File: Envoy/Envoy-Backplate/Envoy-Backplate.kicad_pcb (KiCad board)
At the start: 2 copper layers, 95.4 x 95.4 mm, 13 parts

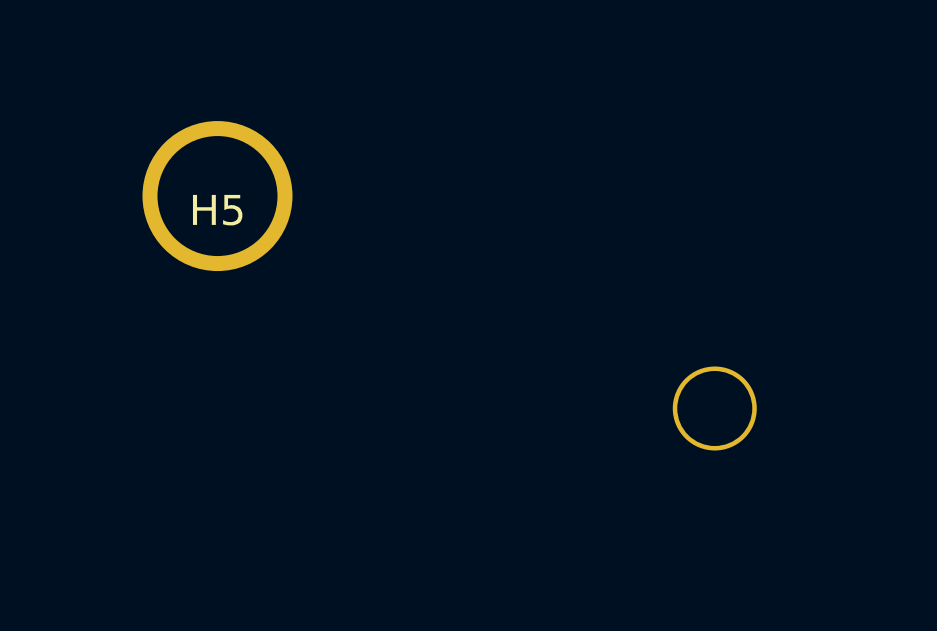
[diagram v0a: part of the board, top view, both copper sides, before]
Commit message: Move standoff and bumper positioning to make the backplate work easier
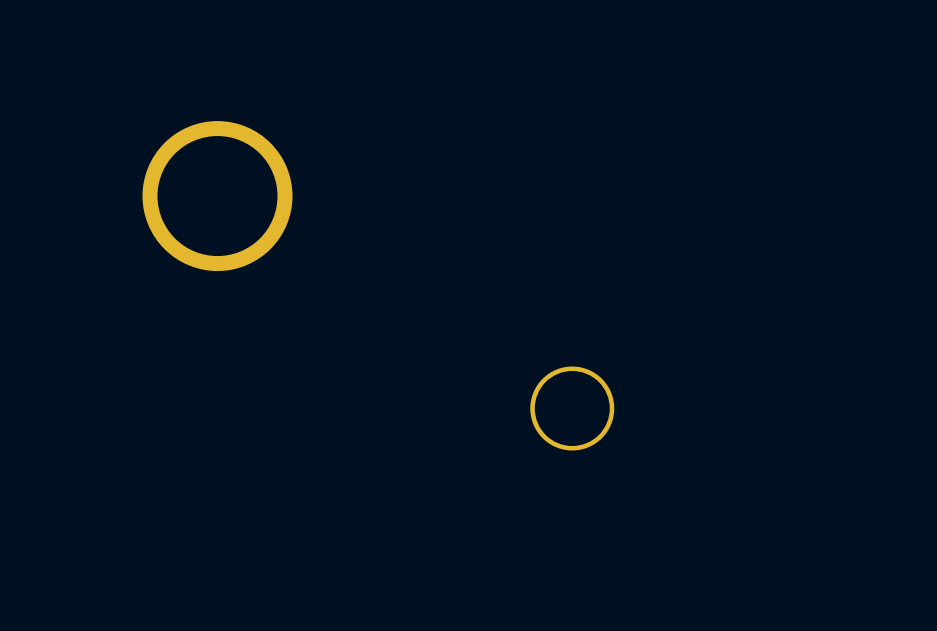
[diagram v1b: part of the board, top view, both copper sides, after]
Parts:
- moved B2 15.7 mm to (111.6, 78.3)
- moved B3 15.7 mm to (169.3, 78.3)
- moved B1 13.9 mm to (111.6, 156.6)
- moved H1 4.75 mm to (123.4, 85.4)
- moved B4 0.84 mm to (169.3, 156.6)

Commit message: add PCB identifier
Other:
- board text added: "Envoy by JeJeff back plate rev 0.2"
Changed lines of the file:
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@@
     (effects (font (size 0.85 0.85) (thickness 0.15)))
+  )
+  (gr_text "Envoy by JeJeff\nback plate\nrev 0.2" (at 182.725 73.844) (layer "F.Mask")
+    (effects (font (size 1 1) (thickness 0.15)) (justify right))
   )
   (zone (net 0) (net_name "") (layer "F.Cu") (hatch edge 0.508)

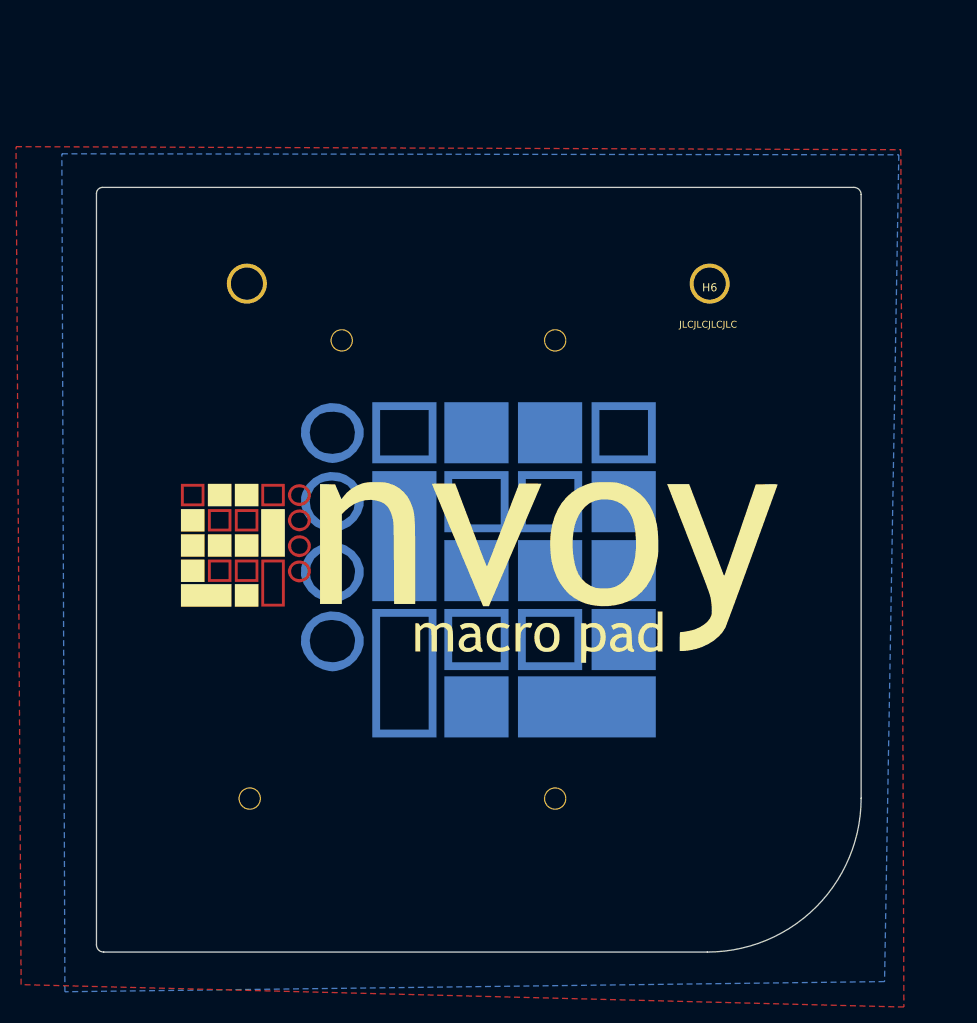
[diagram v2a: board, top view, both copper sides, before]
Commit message: More tweaks to the switchplate cutouts, make switchplate float instead of the PCB, move diodes to give more space to stabs
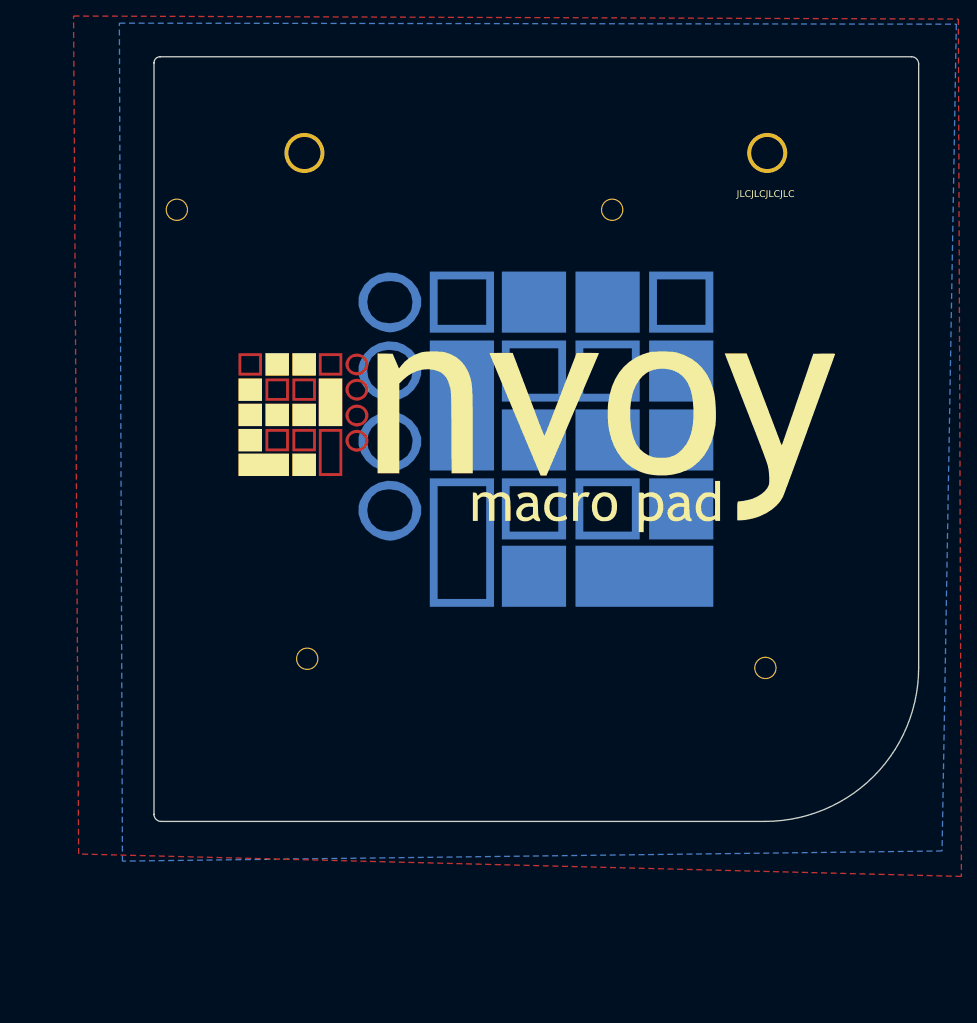
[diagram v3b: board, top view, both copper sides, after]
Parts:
- moved H4 30.9 mm to (176.3, 126.2)
- moved H1 26.2 mm to (102.9, 69.1)
- moved H3 18.9 mm to (119.1, 125.1)
- moved G*** 17.8 mm to (149.5, 97.8)
- moved G*** 17.8 mm to (155.0, 106.1)
- moved B3 17.8 mm to (176.5, 62.0)
- moved H6 17.8 mm to (176.5, 62.0)
- moved B2 17.8 mm to (118.8, 62.0)
- moved H5 17.8 mm to (118.8, 62.0)
- moved B4 17.8 mm to (176.5, 140.3)
- moved G*** 17.8 mm to (147.7, 97.7)
- moved B1 17.8 mm to (118.8, 140.3)
- moved H2 17.8 mm to (157.2, 69.1)

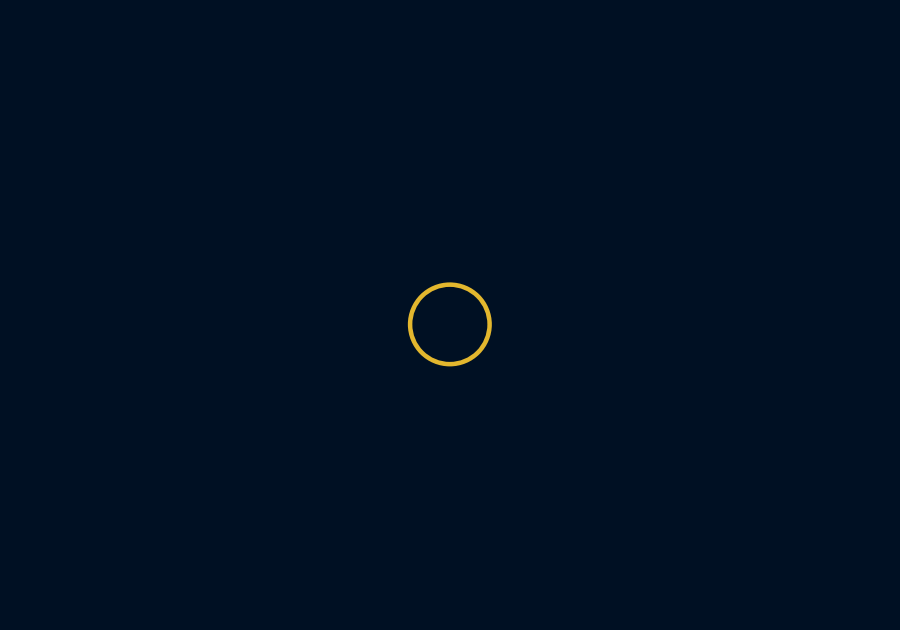
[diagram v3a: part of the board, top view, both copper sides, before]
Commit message: curves!  Fun curved traces.  Prepare rev0.2 gerbers
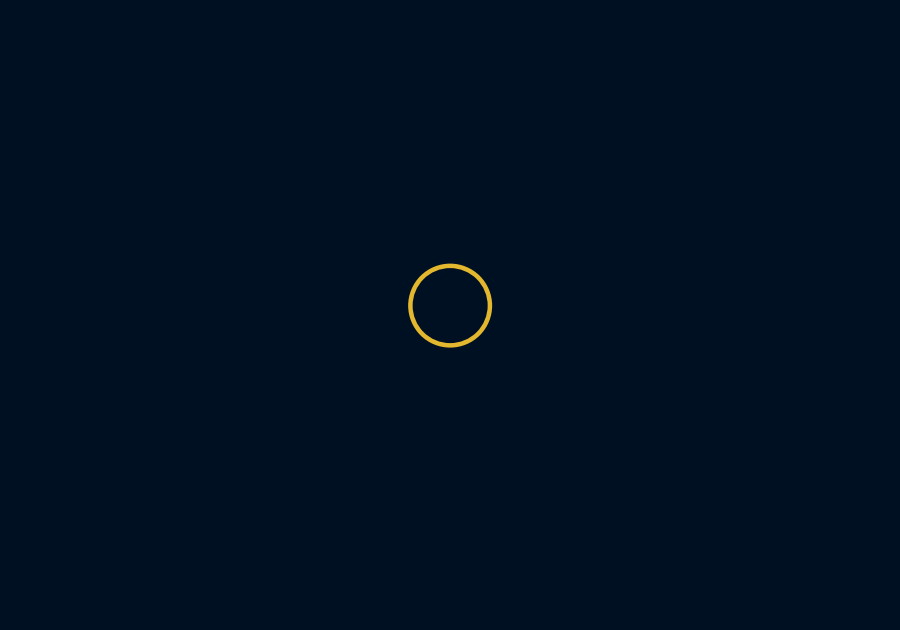
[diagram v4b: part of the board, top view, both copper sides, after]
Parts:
- moved H3 0.63 mm to (119.1, 124.5)
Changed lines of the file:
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@@
   )
   (footprint "Envoy:MountingHole_Reinforced_2.5mm" (layer "F.Cu")
-    (at 119.1255 125.088)
+    (at 119.1355 124.46175)
     (descr "Mounting Hole 2.5mm, no annular")
     (tags "mounting hole 2.5mm no annular")

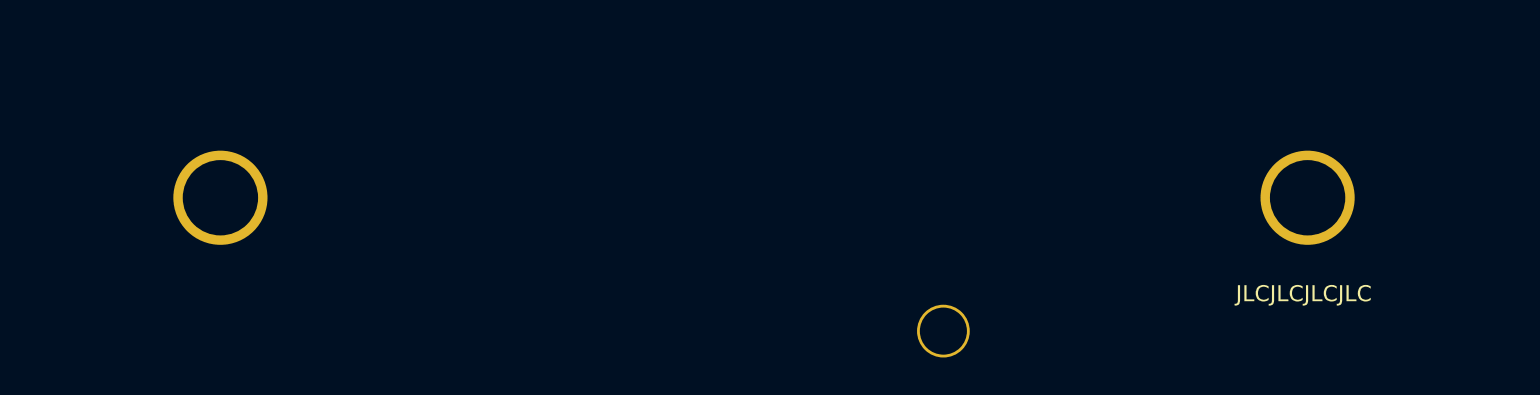
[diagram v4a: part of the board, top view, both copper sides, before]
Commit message: Moved feet outwards a bit for additional stability
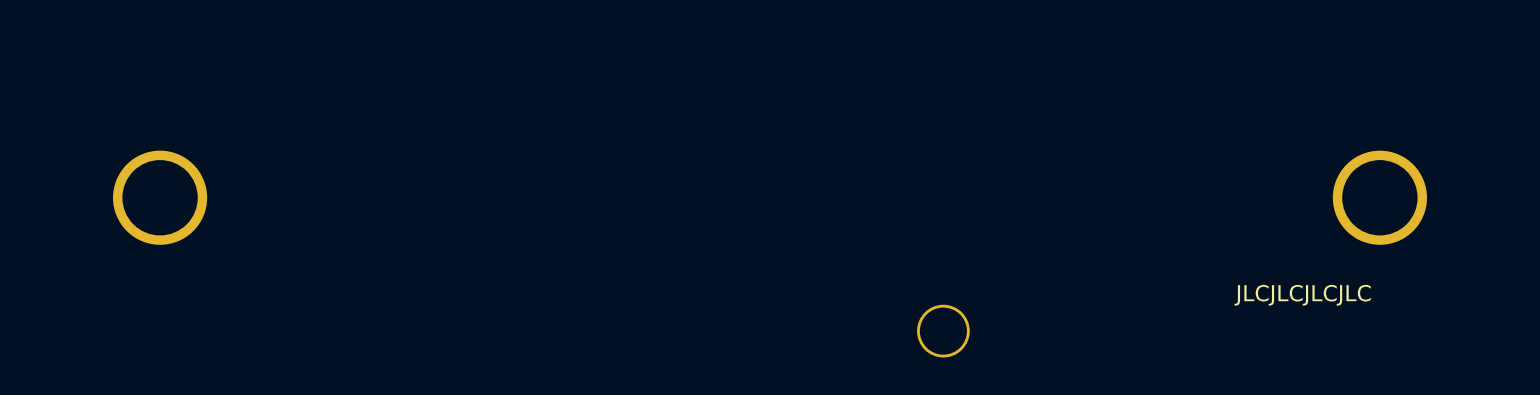
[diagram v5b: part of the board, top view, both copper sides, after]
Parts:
- moved B3 3.84 mm to (180.3, 62.0)
- moved H6 3.84 mm to (180.3, 62.0)
- moved B2 3.20 mm to (115.6, 62.0)
- moved H5 3.20 mm to (115.6, 62.0)

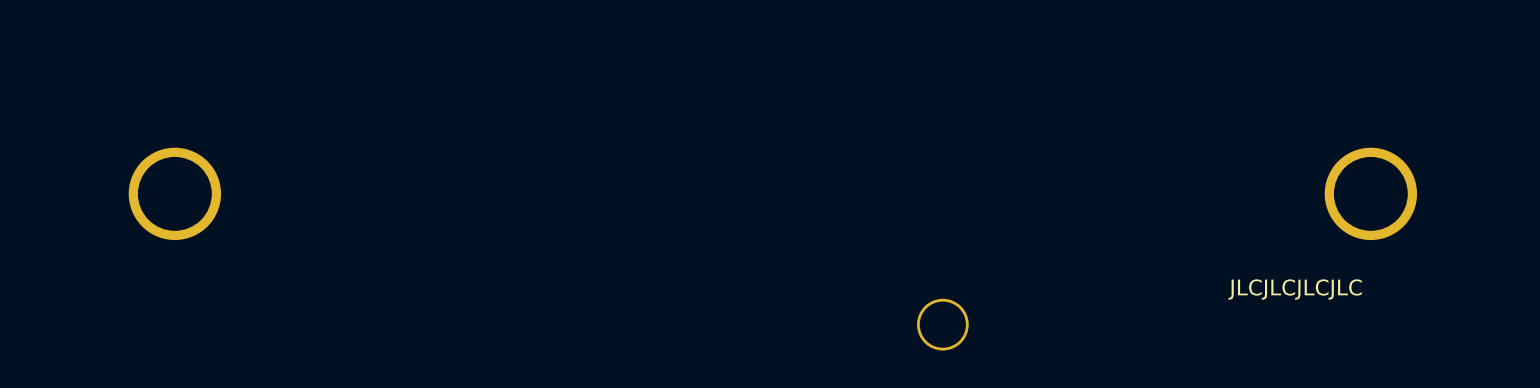
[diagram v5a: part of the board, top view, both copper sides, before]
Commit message: Widen feet placement a little more.  Bump revision to 1.0
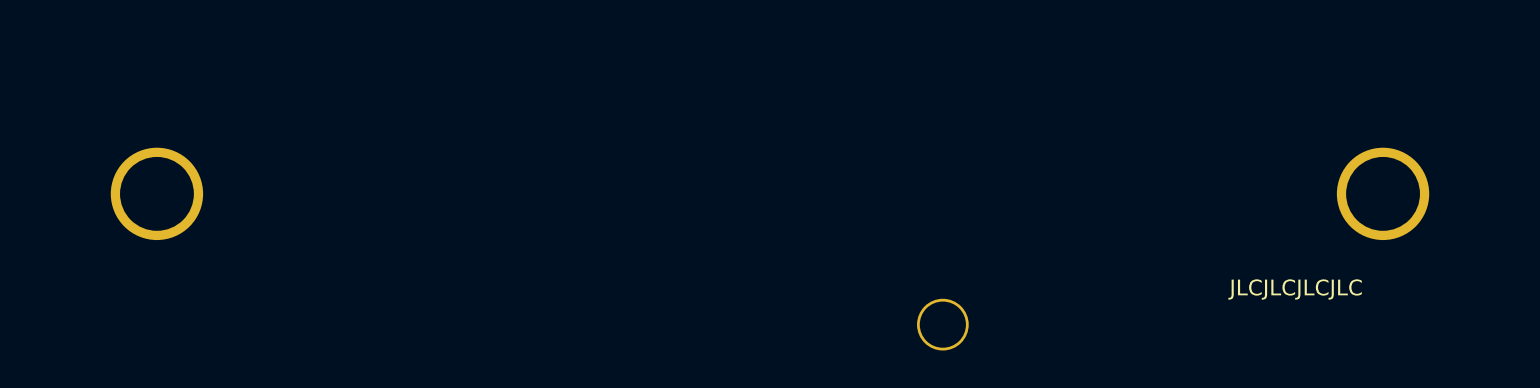
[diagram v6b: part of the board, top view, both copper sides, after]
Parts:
- moved B1 4.17 mm to (114.6, 140.3)
- moved B2 0.97 mm to (114.6, 62.0)
- moved H5 0.97 mm to (114.6, 62.0)
- moved B3 0.66 mm to (181.0, 62.0)
- moved H6 0.66 mm to (181.0, 62.0)
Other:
- board text added: "Envoy by JeJeff back plate rev 1.0"
- board text removed: "Envoy by JeJeff back plate rev 0.2"

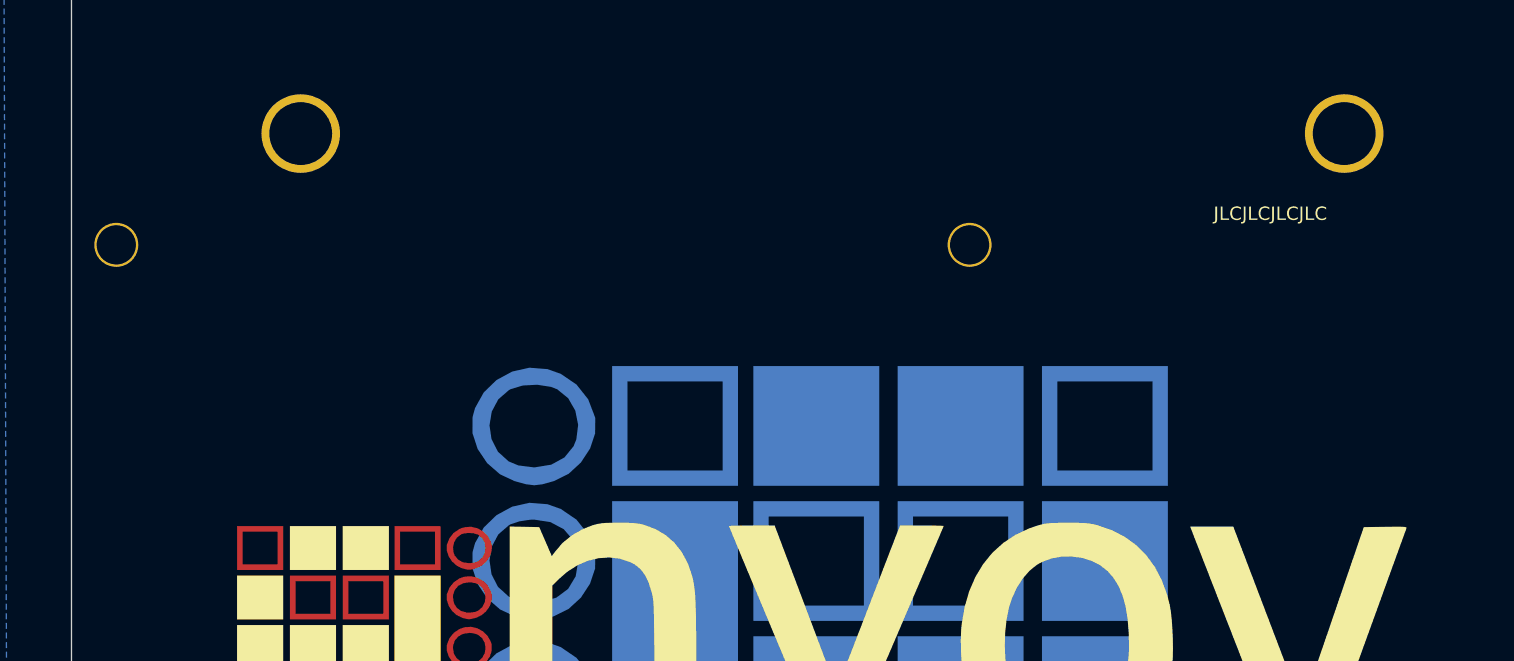
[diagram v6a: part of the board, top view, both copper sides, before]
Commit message: Moved a standoff hole and the feet.  Bumped pcb revision to 1.0
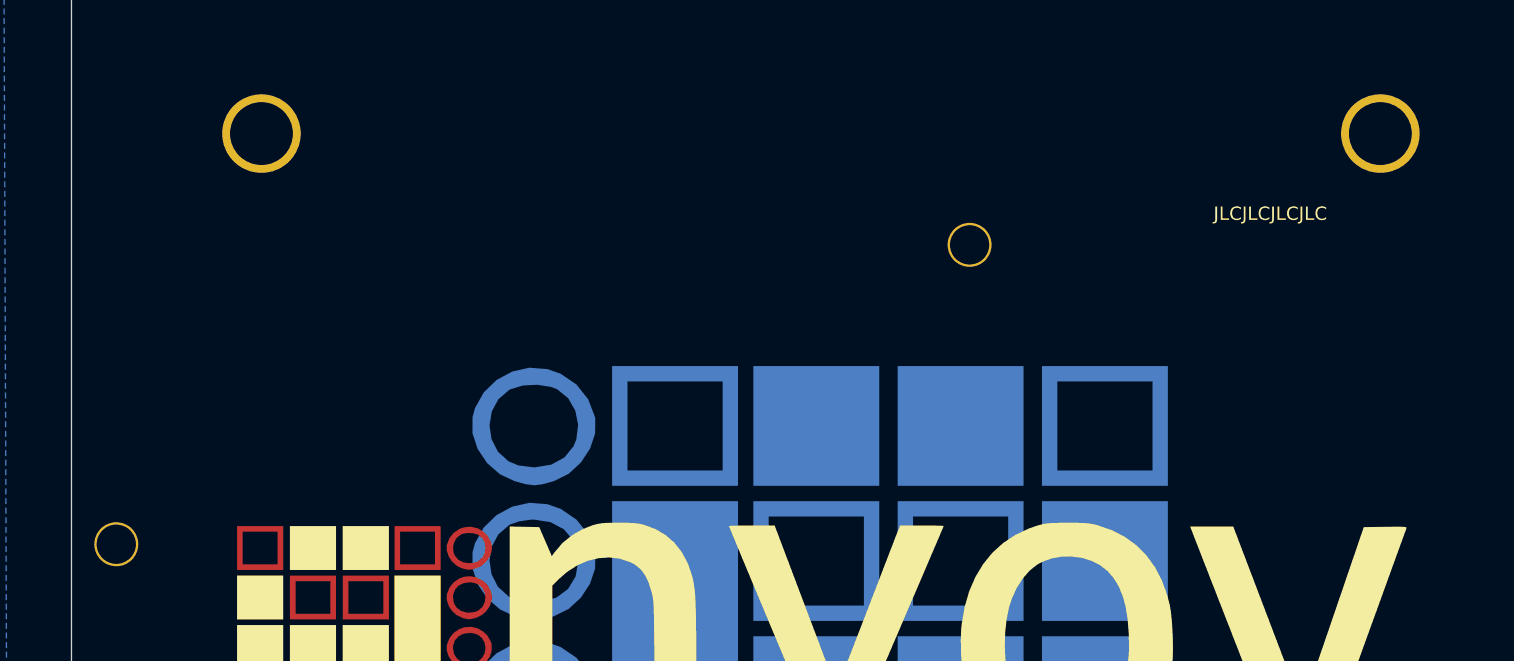
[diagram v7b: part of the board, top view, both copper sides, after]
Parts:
- moved H1 19.0 mm to (102.9, 88.1)
- moved B1 6.70 mm to (107.9, 140.3)
- moved B2 2.50 mm to (112.1, 62.0)
- moved H5 2.50 mm to (112.1, 62.0)
- moved B3 2.30 mm to (183.3, 62.0)
- moved H6 2.30 mm to (183.3, 62.0)
